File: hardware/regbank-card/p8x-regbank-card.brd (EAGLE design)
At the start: 160 x 100 mm, 95 parts, among them J1 FABC96R, U1 P0 L0, U10 P2 L1, U11 P2 H0, U12 P2 H1, U13 P3 L0, U14 P3 L1, U15 P3 H0, U16 P3 H1, U17 PTR SEL 0, U18 PTR SEL 1, U19 PTR SEL 2, U2 P0 L1, U20 PTR SEL 3, U21 PTR SEL 4, U22 PTR SEL 5, U23 PTR SEL 6, U24 PTR SEL 7, U25 ADDR LO, U26 ADDR HI, U27 RDBK LO, U28 RDBK HI, U29 RDBK OUT, U3 P0 H0, U30 DLD DEC, U31 DOE DEC, U32 LOAD DEC, U33 SEL DEC, U34 74HCT02, U35 74HCT14, U36 ZERO P0, U37 74HCT08, U38 74HCT08, U39 CNT DEC, U4 P0 H1, U40 74HCT32, U41 PT LO, U42 PT HI, U43 PT SEL LO, U44 PT SEL HI, U5 P1 L0, U6 P1 L1, U7 P1 H0, U8 P1 H1, U9 P2 L0

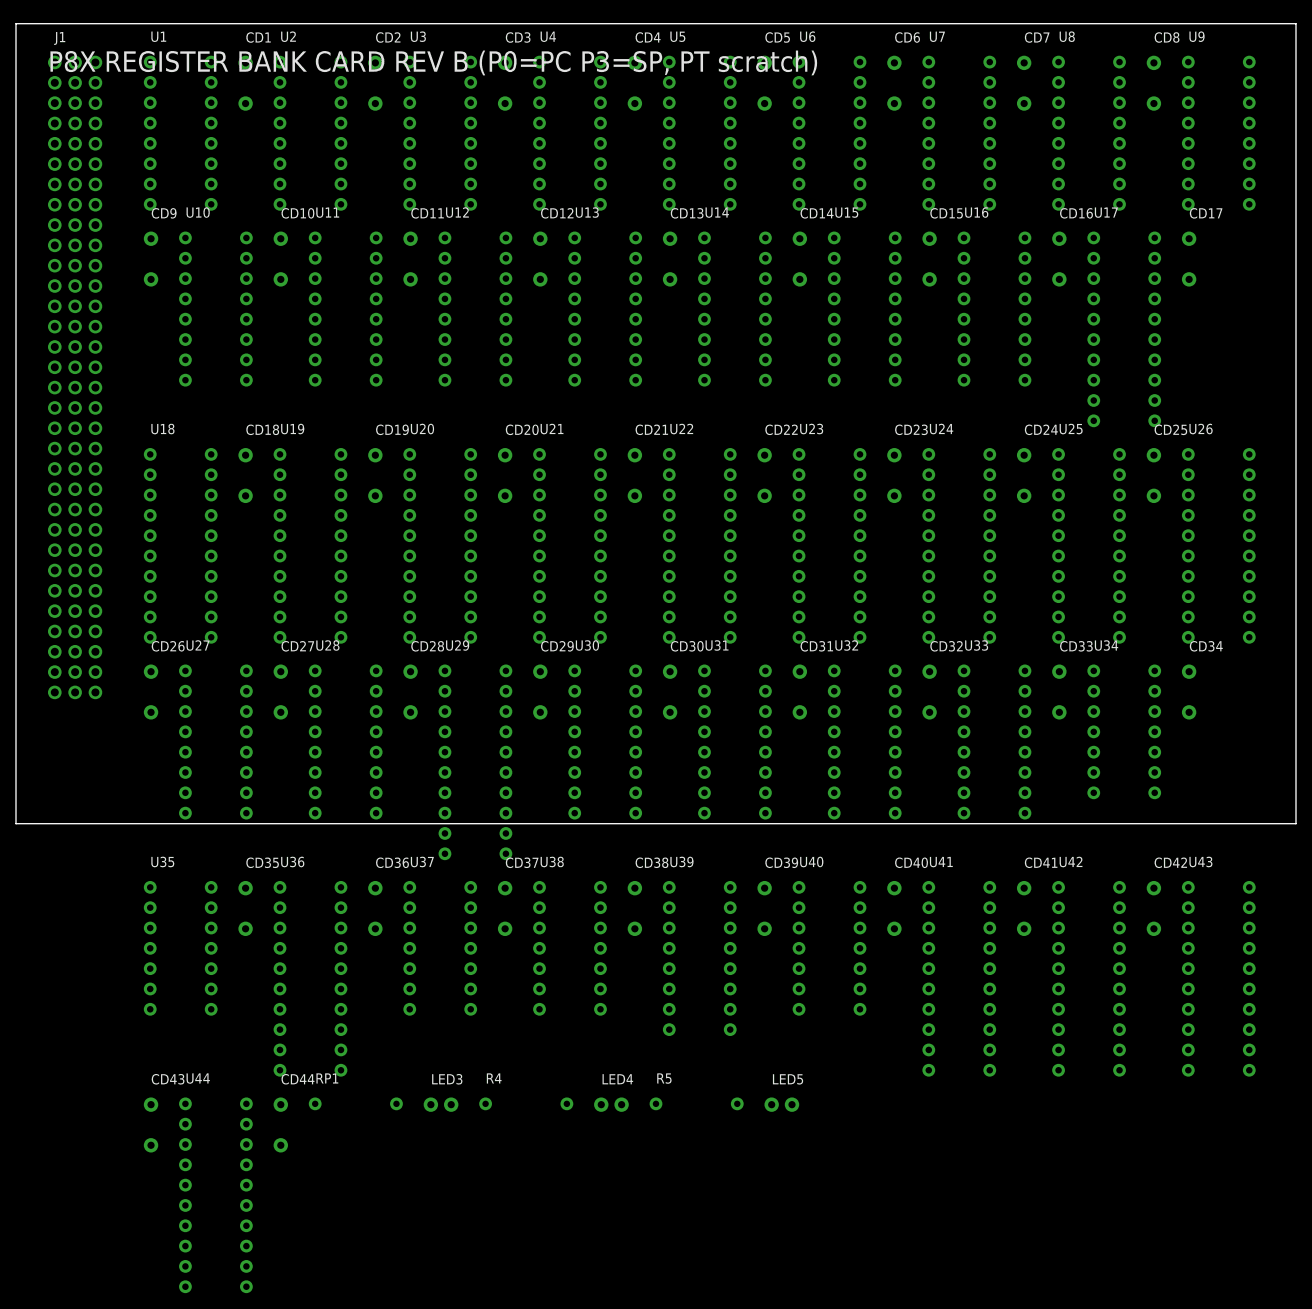
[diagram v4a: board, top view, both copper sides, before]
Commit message: feat(hw): card DIN connector mounting holes (DIN96C, standard DIN 41612)
The card edge connector (FABC96R) needs board mounting holes; the footprint had
only the 96 signal pins. Split the connector into two packages so cards and the
backplane don't share holes:
- DIN96C (card): 96 pins + 2 mounting holes on the centreline (x=2.54), 94.0mm
  apart, drill 2.8mm for M2.5. Emitted as non-plated <hole> elements (new
  lib_xml branch for MH* entries). DEV["DIN96C"] = DIN96 pins, pkg DIN96C.
- DIN96 (backplane receptacle): pins only, unchanged.
Card J1 (all 6: 5 plug-in via card() + memory) now uses DIN96C; backplane slots
keep DIN96. Fixed card() to honor the J1 package on the board side and in CARDS
(was hardcoding "DIN96", which both dropped the holes and mislabeled the BOM).

Verified: each card .brd has 2 holes, backplane 0; overlap guard clean (the
shared-package version collided with backplane terminators); BOM shows 6 card
(DIN96C) + 10 backplane. All boards 0 errors, all 6 suites pass.

VERIFY the 94mm spacing / 2.8mm dia against the FABC96R datasheet.

Co-Authored-By: Claude Opus 4.8 <noreply@anthropic.com>
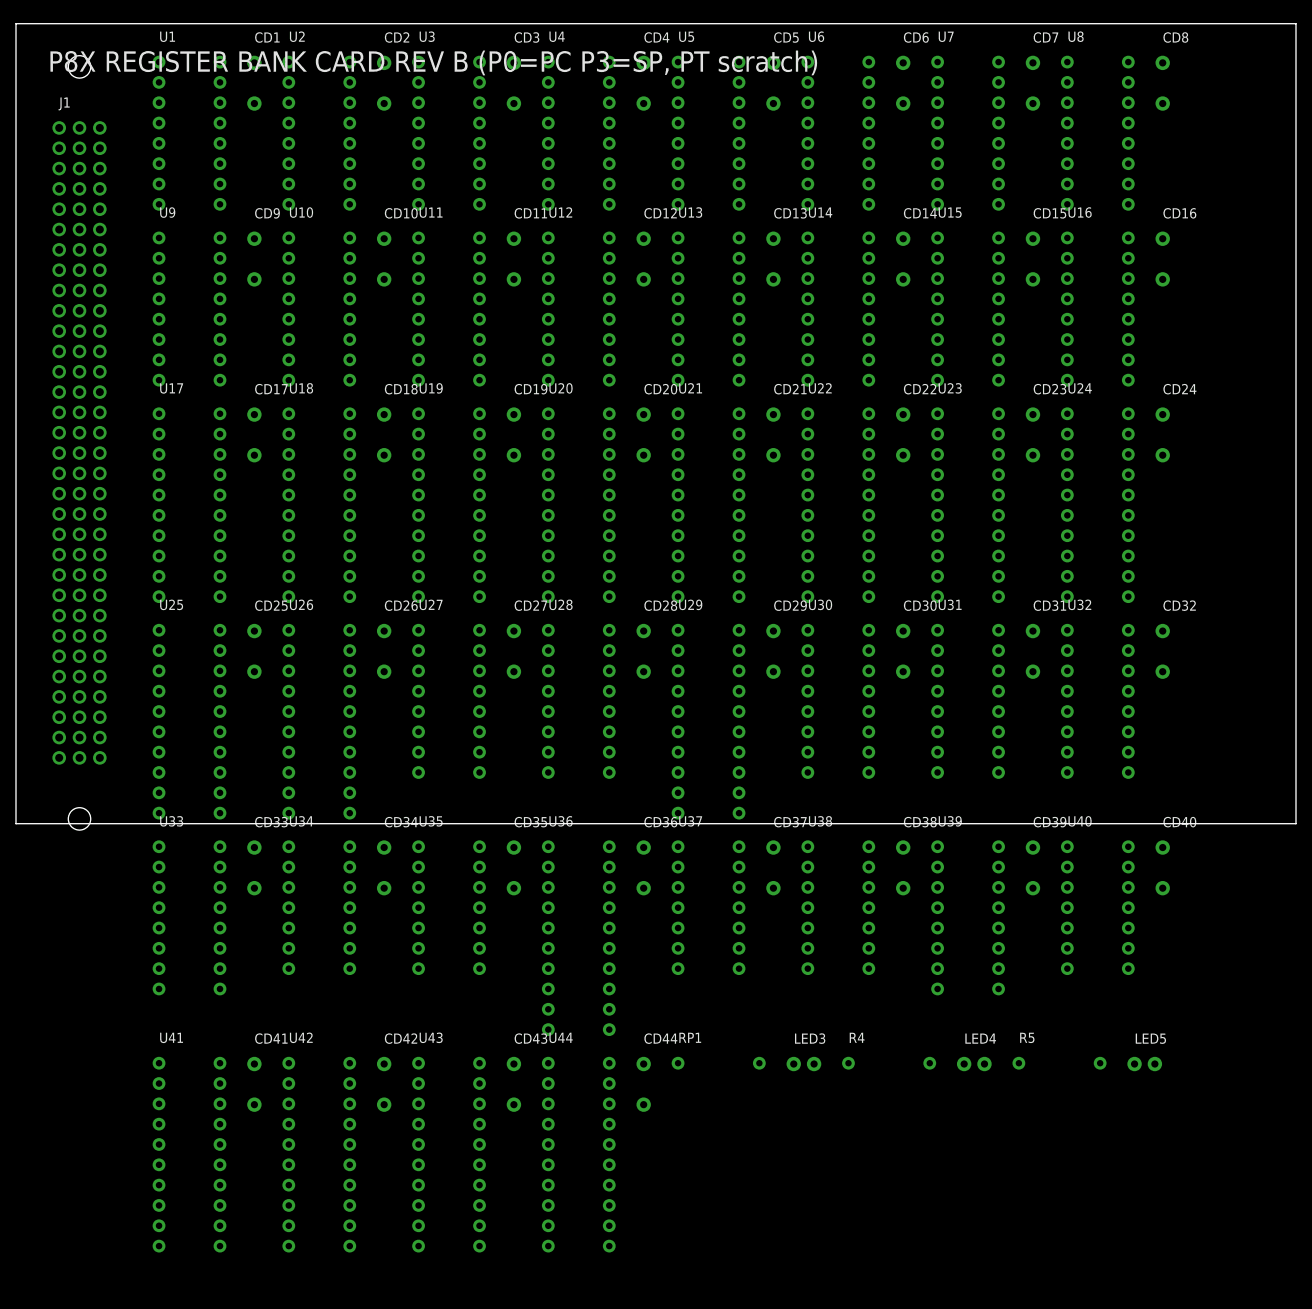
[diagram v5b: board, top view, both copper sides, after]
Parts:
- J1: device p8x:DIN96 -> p8x:DIN96C
- moved U9 130.5 mm to (17.9, 73.2)
- moved U17 118.9 mm to (17.9, 51.2)
- moved CD17 118.9 mm to (29.8, 51.1)
- moved CD25 114.6 mm to (29.8, 24.1)
- moved U25 114.6 mm to (17.9, 24.2)
- moved U26 114.6 mm to (34.1, 24.2)
- moved U33 103.0 mm to (17.9, -2.88)
- moved U34 103.0 mm to (34.1, -2.88)
- moved CD33 103.0 mm to (29.8, -2.98)
- moved CD34 103.0 mm to (46.0, -2.98)
- moved CD41 98.7 mm to (29.8, -30.0)
- moved CD42 98.7 mm to (46.0, -30.0)
- moved U41 98.7 mm to (17.9, -29.9)
- moved U42 98.7 mm to (34.1, -29.9)
- moved U43 98.7 mm to (50.3, -29.9)
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
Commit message: fix(hardware): connect IC power pins on the card()-built boards
Schematic-review fix. card() wired the edge-connector and decoupling-cap pins to
VCC/GND but never added each IC's own VCC/GND supply pin, so on control, regbank,
ALU, I/O, and CF the chips' power pads were not members of the power pours and
would not have been powered. (The hand-built memory card already did this; the
backplane has no ICs. validate() couldn't catch it — it checks pin-name legality,
not connectivity.)

- card(): append (ref,"VCC")/(ref,"GND") for every IC, skipping any pin already
  wired by hand (idempotent — avoids duplicate pinrefs, e.g. ALU U16 GND)
- regenerated all 7 boards (.sch/.brd), 0 validation errors
- board-level audit: every IC on every card now has both VCC and GND on the
  power signals
- BACKLOG: moved the critical item to DONE; theory docs' power-pin callouts
  updated to "fixed"

Co-Authored-By: Claude Opus 4.8 <noreply@anthropic.com>
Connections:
- net GND: now also U1.8, U10.8, U11.8, U12.8, U13.8, U14.8, U15.8, U16.8, U17.10, U18.10, U19.10, U2.8, U20.10, U21.10, U22.10, U23.10, U24.10, U25.10, U26.10, U27.8, U28.8, U29.10, U3.8, U30.8, U31.8, U32.8, U33.8, U34.7, U35.7, U36.10, U37.7, U38.7, U39.8, U4.8, U40.7, U41.10, U42.10, U43.10, U44.10, U5.8, U6.8, U7.8, U8.8, U9.8
- net VCC: now also U1.16, U10.16, U11.16, U12.16, U13.16, U14.16, U15.16, U16.16, U17.20, U18.20, U19.20, U2.16, U20.20, U21.20, U22.20, U23.20, U24.20, U25.20, U26.20, U27.16, U28.16, U29.20, U3.16, U30.16, U31.16, U32.16, U33.16, U34.14, U35.14, U36.20, U37.14, U38.14, U39.16, U4.16, U40.14, U41.20, U42.20, U43.20, U44.20, U5.16, U6.16, U7.16, U8.16, U9.16
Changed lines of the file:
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@@
 <contactref element="CD43" pad="2"/>
 <contactref element="CD44" pad="2"/>
+<contactref element="U1" pad="8"/>
+<contactref element="U2" pad="8"/>
+<contactref element="U3" pad="8"/>
+<contactref element="U4" pad="8"/>
+<contactref element="U5" pad="8"/>
+<contactref element="U6" pad="8"/>
+<contactref element="U7" pad="8"/>
+<contactref element="U8" pad="8"/>
+<contactref element="U9" pad="8"/>
+<contactref element="U10" pad="8"/>
+<contactref element="U11" pad="8"/>
+<contactref element="U12" pad="8"/>
+<contactref element="U13" pad="8"/>
+<contactref element="U14" pad="8"/>
+<contactref element="U15" pad="8"/>
+<contactref element="U16" pad="8"/>
+<contactref element="U17" pad="10"/>
+<contactref element="U18" pad="10"/>
+<contactref element="U19" pad="10"/>
+<contactref element="U20" pad="10"/>
+<contactref element="U21" pad="10"/>
+<contactref element="U22" pad="10"/>
+<contactref element="U23" pad="10"/>
+<contactref element="U24" pad="10"/>
+<contactref element="U25" pad="10"/>
+<contactref element="U26" pad="10"/>
+<contactref element="U27" pad="8"/>
+<contactref element="U28" pad="8"/>
+<contactref element="U29" pad="10"/>
+<contactref element="U30" pad="8"/>
+<contactref element="U31" pad="8"/>
+<contactref element="U32" pad="8"/>
+<contactref element="U33" pad="8"/>
+<contactref element="U34" pad="7"/>
+<contactref element="U35" pad="7"/>
+<contactref element="U36" pad="10"/>
+<contactref element="U37" pad="7"/>
+<contactref element="U38" pad="7"/>
+<contactref element="U39" pad="8"/>
+<contactref element="U40" pad="7"/>
+<contactref element="U41" pad="10"/>
+<contactref element="U42" pad="10"/>
+<contactref element="U43" pad="10"/>
+<contactref element="U44" pad="10"/>
 <polygon width="0.254" layer="2" isolate="0.3" rank="1">
 <vertex x="0" y="0"/>
@@
 <contactref element="CD43" pad="1"/>
 <contactref element="CD44" pad="1"/>
+<contactref element="U1" pad="16"/>
+<contactref element="U2" pad="16"/>
+<contactref element="U3" pad="16"/>
+<contactref element="U4" pad="16"/>
+<contactref element="U5" pad="16"/>
+<contactref element="U6" pad="16"/>
+<contactref element="U7" pad="16"/>
+<contactref element="U8" pad="16"/>
+<contactref element="U9" pad="16"/>
+<contactref element="U10" pad="16"/>
+<contactref element="U11" pad="16"/>
+<contactref element="U12" pad="16"/>
+<contactref element="U13" pad="16"/>
+<contactref element="U14" pad="16"/>
+<contactref element="U15" pad="16"/>
+<contactref element="U16" pad="16"/>
+<contactref element="U17" pad="20"/>
+<contactref element="U18" pad="20"/>
+<contactref element="U19" pad="20"/>
+<contactref element="U20" pad="20"/>
+<contactref element="U21" pad="20"/>
+<contactref element="U22" pad="20"/>
+<contactref element="U23" pad="20"/>
+<contactref element="U24" pad="20"/>
+<contactref element="U25" pad="20"/>
+<contactref element="U26" pad="20"/>
+<contactref element="U27" pad="16"/>
+<contactref element="U28" pad="16"/>
+<contactref element="U29" pad="20"/>
+<contactref element="U30" pad="16"/>
+<contactref element="U31" pad="16"/>
+<contactref element="U32" pad="16"/>
+<contactref element="U33" pad="16"/>
+<contactref element="U34" pad="14"/>
+<contactref element="U35" pad="14"/>
+<contactref element="U36" pad="20"/>
+<contactref element="U37" pad="14"/>
+<contactref element="U38" pad="14"/>
+<contactref element="U39" pad="16"/>
+<contactref element="U40" pad="14"/>
+<contactref element="U41" pad="20"/>
+<contactref element="U42" pad="20"/>
+<contactref element="U43" pad="20"/>
+<contactref element="U44" pad="20"/>
 <polygon width="0.254" layer="15" isolate="0.3" rank="1">
 <vertex x="0" y="0"/>

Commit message: feat(backplane): row-B even pins become spare bus lines (SPARE12-23)
Row B was a solid ground guard (B3-26 all GND). Per request, B3-26 now ALTERNATE:
odd pins stay GND (still a guard between most signal pairs), and the 12 even pins
(B4,B6,..,B26) become spare bus lines SPARE12-SPARE23, routed slot-to-slot — so
new signals can be added later without re-spinning the backplane. B27-30
(CLRC/BSEL/IRQ/SPARE11) unchanged.

- busnet() updated in all three copies (gen_eagle, gen_bus_pdf, gen_bus_card)
- backplane .brd routes the 12 new spares (mirrors the B27-30 routing); odd-pin
  grounds remain on the GND pour
- every card regenerated: their connectors no longer tie the even B pins to GND
  (those are spare lines now) — they simply don't connect the spares
- all 8 boards validate (0 errors); schematic + bus PDFs regenerated
- docs updated: bus-definition (pin map + notes), backplane theory + design notes
- net signal-integrity trade noted: a solid guard shields slightly better; the
  alternation was chosen deliberately for expansion room

Co-Authored-By: Claude Opus 4.8 <noreply@anthropic.com>
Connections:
- net GND: no longer J1.B10, J1.B12, J1.B14, J1.B16, J1.B18, J1.B20, J1.B22, J1.B24, J1.B26, J1.B4, J1.B6, J1.B8
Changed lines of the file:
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@@
 <contactref element="J1" pad="A32"/>
 <contactref element="J1" pad="B3"/>
-<contactref element="J1" pad="B4"/>
 <contactref element="J1" pad="B5"/>
-<contactref element="J1" pad="B6"/>
 <contactref element="J1" pad="B7"/>
-<contactref element="J1" pad="B8"/>
 <contactref element="J1" pad="B9"/>
-<contactref element="J1" pad="B10"/>
 <contactref element="J1" pad="B11"/>
-<contactref element="J1" pad="B12"/>
 <contactref element="J1" pad="B13"/>
-<contactref element="J1" pad="B14"/>
 <contactref element="J1" pad="B15"/>
-<contactref element="J1" pad="B16"/>
 <contactref element="J1" pad="B17"/>
-<contactref element="J1" pad="B18"/>
 <contactref element="J1" pad="B19"/>
-<contactref element="J1" pad="B20"/>
 <contactref element="J1" pad="B21"/>
-<contactref element="J1" pad="B22"/>
 <contactref element="J1" pad="B23"/>
-<contactref element="J1" pad="B24"/>
 <contactref element="J1" pad="B25"/>
-<contactref element="J1" pad="B26"/>
 <contactref element="J1" pad="B31"/>
 <contactref element="J1" pad="B32"/>
